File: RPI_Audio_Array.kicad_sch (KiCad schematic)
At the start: 40 parts, among them J1 Conn_02x20_Odd_Even, U1 PCMD3140IRTER, U2 SPH0690LM4H-1, U3 SPH0690LM4H-1, U4 SPH0690LM4H-1, U5 SPH0690LM4H-1, U6 TLV7103318QDSERQ1

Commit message: Fix: Schemtatic fixes
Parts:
- added C21, C22, C23, C24, C25: 2.2uf, Capacitor_SMD:C_0805_2012Metric, symbol Device:C
- added C26: 100nf, Capacitor_SMD:C_1206_3216Metric, symbol Device:C
- added C27: 1nf, Capacitor_SMD:C_0805_2012Metric, symbol Device:C
- added C28: 100pf, Capacitor_SMD:C_0805_2012Metric, symbol Device:C
- added C29: 10uf, Capacitor_SMD:C_1206_3216Metric, symbol Device:C
- added R3, R5: 470, Resistor_SMD:R_0201_0603Metric, symbol Device:R
- C11, C12, C5: lcsc (none) -> CL10C331JB8NNNC
- C13: value 1uf -> 10nf; footprint Capacitor_SMD:C_0603_1608Metric -> Capacitor_SMD:C_01005_0402Metric; lcsc CL10A105KB8NNNC -> CL05B103KB5NNNC
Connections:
- net VDD is gone; now on net +3.3V: U2.2 (SELECT), U4.2 (SELECT)
- net +3.3V: now also R3.2, R5.2; no longer U1.16 (AVDD)
- net +5V: now also C26.1, C27.1, C28.1, C29.1
- net GND: now also C21.2, C22.2, C23.2, C24.2, C25.2, C26.2, C27.2, C28.2, C29.2; no longer FB1.2
- net SCL: now also R5.1
- net SDA: now also R3.1
- net at C10.1, C12.1, C4.1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: now also C21.1
- net at C6.1, C7.1, C8.1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: now also C24.1
- net at C2.1, C3.1, C5.1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: now also C23.1
- net at C1.1, C11.1, C9.1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: now also C22.1
- new net AVDD: C25.1, FB1.2, U1.16 (AVDD)
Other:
- note added: "Bulk"
- note added: "Decoupling"
- moved on the sheet: C1, C10, C11, C12, C13, C4, C9, FB1, FB4, FB5, R8, R9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

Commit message: Chore: Updating PCB
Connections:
- net GPIO1 renamed PCMD_GPIO1
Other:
- note added: "Figure 3 shows SDOUT wired to SDIN of Pi"
- note added: "Shows PCM in is GPIO20"
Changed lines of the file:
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@@
   (junction (at 41.91 31.75) (diameter 0) (color 0 0 0 0)
-  )
-  (junction (at 143.51 110.49) (diameter 0) (color 0 0 0 0)
   )
   (no_connect (at 156.21 181.61))
@@
     (stroke (width 0) (type default))
   )
-  (wire (pts (xy 144.78 110.49) (xy 143.51 110.49))
-    (stroke (width 0) (type default))
-  )
   (wire (pts (xy 152.4 35.56) (xy 166.37 35.56))
     (stroke (width 0) (type default))
@@
     (stroke (width 0) (type default))
   )
+  (wire (pts (xy 139.7 110.49) (xy 143.51 110.49))
+    (stroke (width 0) (type default))
+  )
   (wire (pts (xy 25.4 99.06) (xy 33.02 99.06))
     (stroke (width 0) (type default))
@@
   )
   (wire (pts (xy 264.16 95.25) (xy 264.16 99.06))
-    (stroke (width 0) (type default))
-  )
-  (wire (pts (xy 143.51 110.49) (xy 139.7 110.49))
     (stroke (width 0) (type default))
   )
@@
     (effects (font (size 1.27 1.27)) (justify left bottom))
   )
+  (text "Figure 3 shows SDOUT wired to SDIN of Pi" (at 176.53 148.59 0)
+    (effects (font (size 1.27 1.27)) (justify left bottom) (href "https://www.analog.com/media/en/technical-documentation/technical-articles/ms-2275.pdf"))
+  )
+  (text "Shows PCM in is GPIO20" (at 176.53 152.4 0)
+    (effects (font (size 1.27 1.27)) (justify left bottom) (href "https://raspberrypi.stackexchange.com/questions/79870/confirming-the-i2s-pins-on-raspberry-pi-3-model-b"))
+  )
   (text "Decoupling" (at 25.4 151.13 0)
     (effects (font (size 1.27 1.27)) (justify left bottom))
@@
     )
   )
-  (global_label "GPIO1" (shape input) (at 231.14 107.95 0) (fields_autoplaced)
-    (effects (font (size 1.27 1.27)) (justify left))
-    (property "Intersheetrefs" "${INTERSHEET_REFS}" (at 239.81 107.95 0)
+  (global_label "PCMD_GPIO1" (shape input) (at 231.14 107.95 0) (fields_autoplaced)
+    (effects (font (size 1.27 1.27)) (justify left))
+    (property "Intersheetrefs" "${INTERSHEET_REFS}" (at 246.039 107.95 0)
       (effects (font (size 1.27 1.27)) (justify left) hide)
     )
@@
     )
   )
-  (global_label "GPIO1" (shape input) (at 143.51 181.61 180) (fields_autoplaced)
-    (effects (font (size 1.27 1.27)) (justify right))
-    (property "Intersheetrefs" "${INTERSHEET_REFS}" (at 134.84 181.61 0)
-      (effects (font (size 1.27 1.27)) (justify right) hide)
-    )
+  (global_label "PCMD_GPIO1" (shape input) (at 143.51 181.61 180) (fields_autoplaced)
+    (effects (font (size 1.27 1.27)) (justify right))
+    (property "Intersheetrefs" "${INTERSHEET_REFS}" (at 128.611 181.61 0)
+      (effects (font (size 1.27 1.27)) (justify right) hide)
+    )

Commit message: Fix: making further changes to bugs in schematic
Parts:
- added C30: 10uf, Capacitor_SMD:C_1206_3216Metric, symbol Device:C
- added C31, C35, C36: 100nf, Capacitor_SMD:C_1206_3216Metric, symbol Device:C
- added C32: 10nf, Capacitor_SMD:C_01005_0402Metric, symbol Device:C
- added C33: 1nf, Capacitor_SMD:C_0805_2012Metric, symbol Device:C
- added C34: 100pf, Capacitor_SMD:C_0805_2012Metric, symbol Device:C
- C25: value 2.2uf -> 100nf; footprint Capacitor_SMD:C_0805_2012Metric -> Capacitor_SMD:C_1206_3216Metric; lcsc CL21A225KBQNNNE -> CL31B104KBCNNNC
- R3, R5: value 470 -> 4K7
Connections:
- net +1V8: now also C30.1, C31.1, C32.1, C33.1, C34.1
- net +3.3V: now also C25.1; no longer C14.1, U2.2 (SELECT), U4.2 (SELECT)
- net +5V: no longer C13.1, C26.1, C27.1, C28.1, C29.1
- net AVDD: now also C13.1, C14.1, C26.1, C27.1, C28.1, C29.1, C36.1; no longer C25.1
- net GND: now also C30.2, C31.2, C32.2, C33.2, C34.2, C35.2, C36.2
- net SELECT_2: now reaches C24.1, C6.1, C7.1, C8.1, FB2.1, U2.5 (VDD)
- net SELECT_2: now also U2.2 (SELECT)
- net SELECT_1: now reaches C1.1, C11.1, C22.1, C9.1, FB4.1, U4.5 (VDD)
- net SELECT_1: now also U4.2 (SELECT)
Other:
- moved on the sheet: C13, C14, C15, C16, C17, C18, C19, C20, C26, C27, C28, C29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

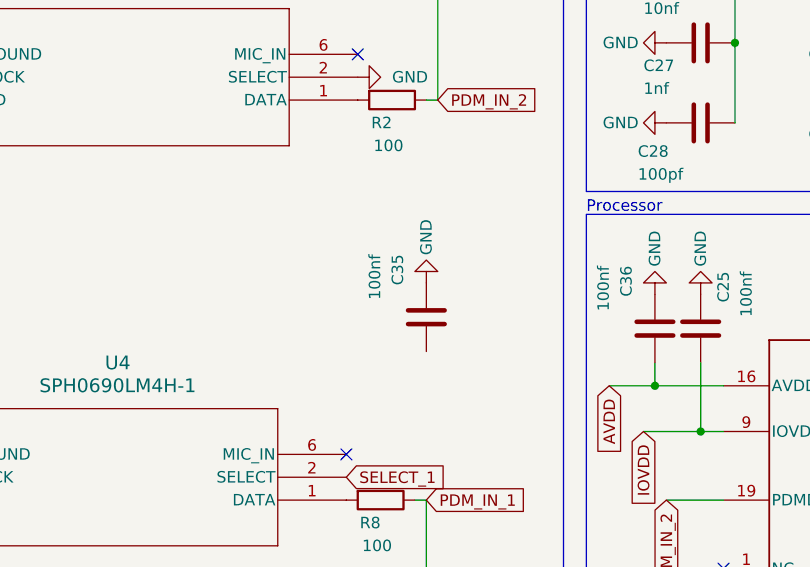
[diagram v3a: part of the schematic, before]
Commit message: Fix: Removing extra cap
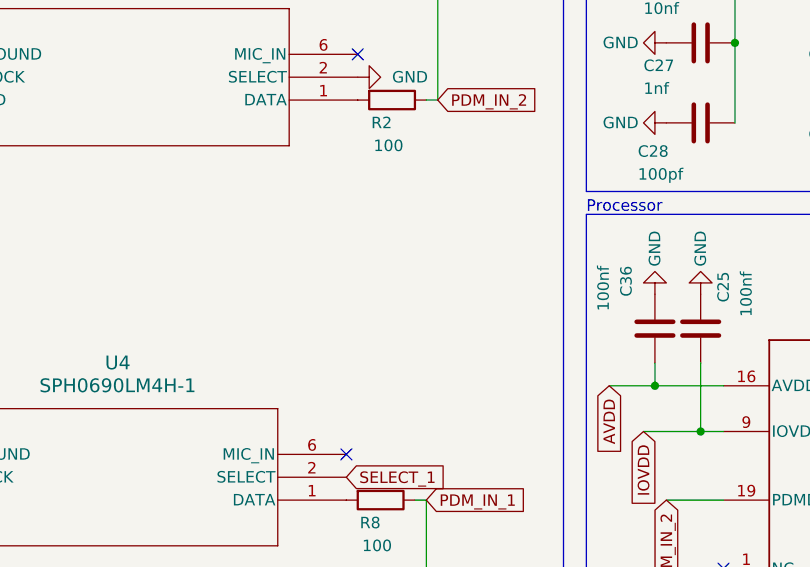
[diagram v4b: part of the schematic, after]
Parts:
- removed C35: 100nf, Capacitor_SMD:C_1206_3216Metric, symbol Device:C
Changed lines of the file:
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@@
-    )
-  )
-  (symbol (lib_id "power:GND") (at 110.49 74.93 180) (unit 1)
-    (in_bom yes) (on_board yes) (dnp no)
-    (property "Reference" "#PWR038" (at 110.49 68.58 0)
-      (effects (font (size 1.27 1.27)) hide)
-    )
-    (property "Value" "GND" (at 110.49 69.85 90)
-      (effects (font (size 1.27 1.27)))
-    )
-    (property "Footprint" "" (at 110.49 74.93 0)
-      (effects (font (size 1.27 1.27)) hide)
-    )
-    (property "Datasheet" "" (at 110.49 74.93 0)
-      (effects (font (size 1.27 1.27)) hide)
-    )
-    (pin "1")
-    (instances
-      (project "RPI_Audio_Array"
-        (path "/954bfd10-59e4-4b5e-a9fc-5f77bd6479b0"
-          (reference "#PWR038") (unit 1)
-        )
-      )
     )
   )
@@
         )
       )
-    )
-  )
-  (symbol (lib_id "Device:C") (at 110.49 78.74 180) (unit 1)
-    (in_bom yes) (on_board yes) (dnp no)
-    (property "Reference" "C35" (at 107.315 71.755 90)
-      (effects (font (size 1.27 1.27)) (justify left))
-    )
-    (property "Value" "100nf" (at 104.775 71.755 90)
-      (effects (font (size 1.27 1.27)) (justify left))
-    )
-    (property "Footprint" "Capacitor_SMD:C_1206_3216Metric" (at 109.5248 74.93 0)
-      (effects (font (size 1.27 1.27)) hide)
-    )
-    (property "Datasheet" "https://jlcpcb.com/partdetail/25237-CL31B104KBCNNNC/C24497" (at 110.49 78.74 0)
-      (effects (font (size 1.27 1.27)) hide)
-    )
-    (property "lcsc" "CL31B104KBCNNNC" (at 110.49 78.74 0)
-      (effects (font (size 1.27 1.27)) hide)
-    )
-    (pin "1")
-    (pin "2")
-    (instances
-      (project "RPI_Audio_Array"
-        (path "/954bfd10-59e4-4b5e-a9fc-5f77bd6479b0"
-          (reference "C35") (unit 1)
-        )
-      )

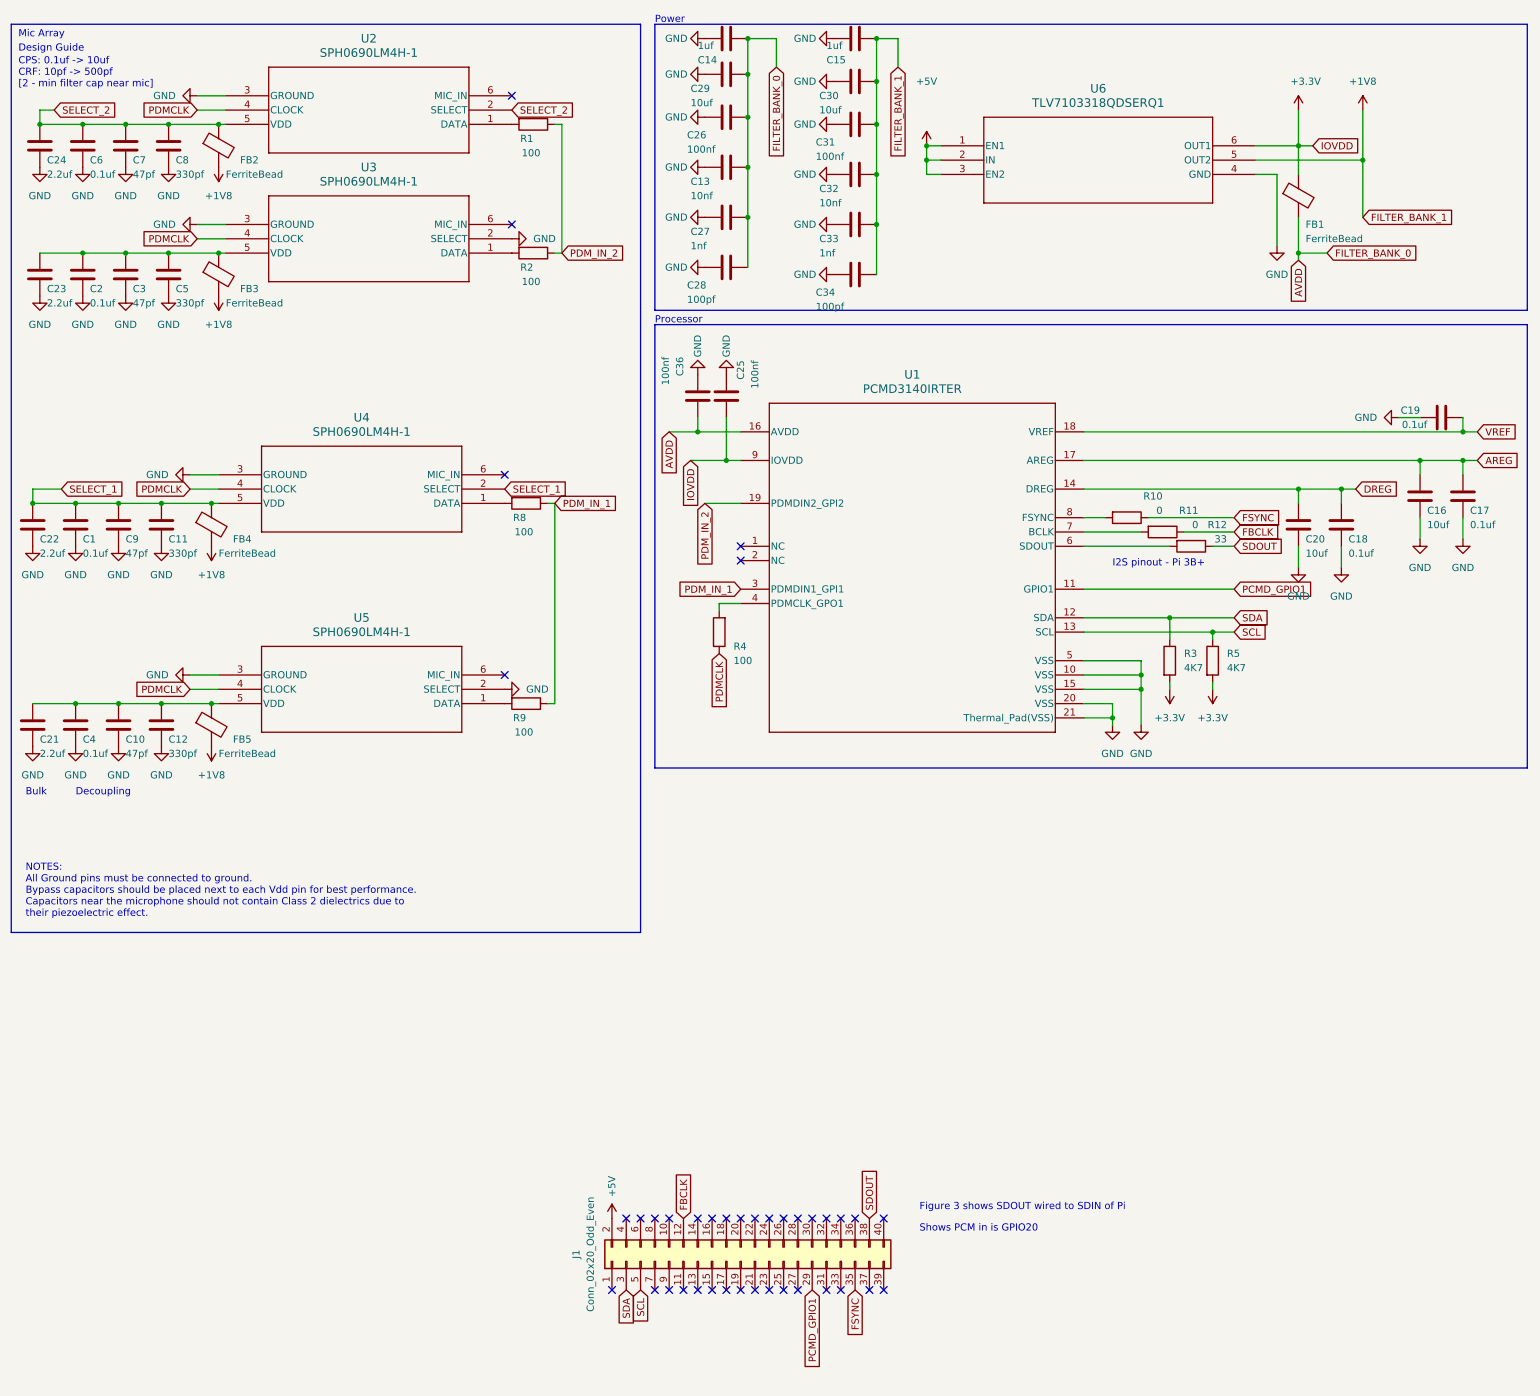
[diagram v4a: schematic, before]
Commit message: Chore: To fix drc issues
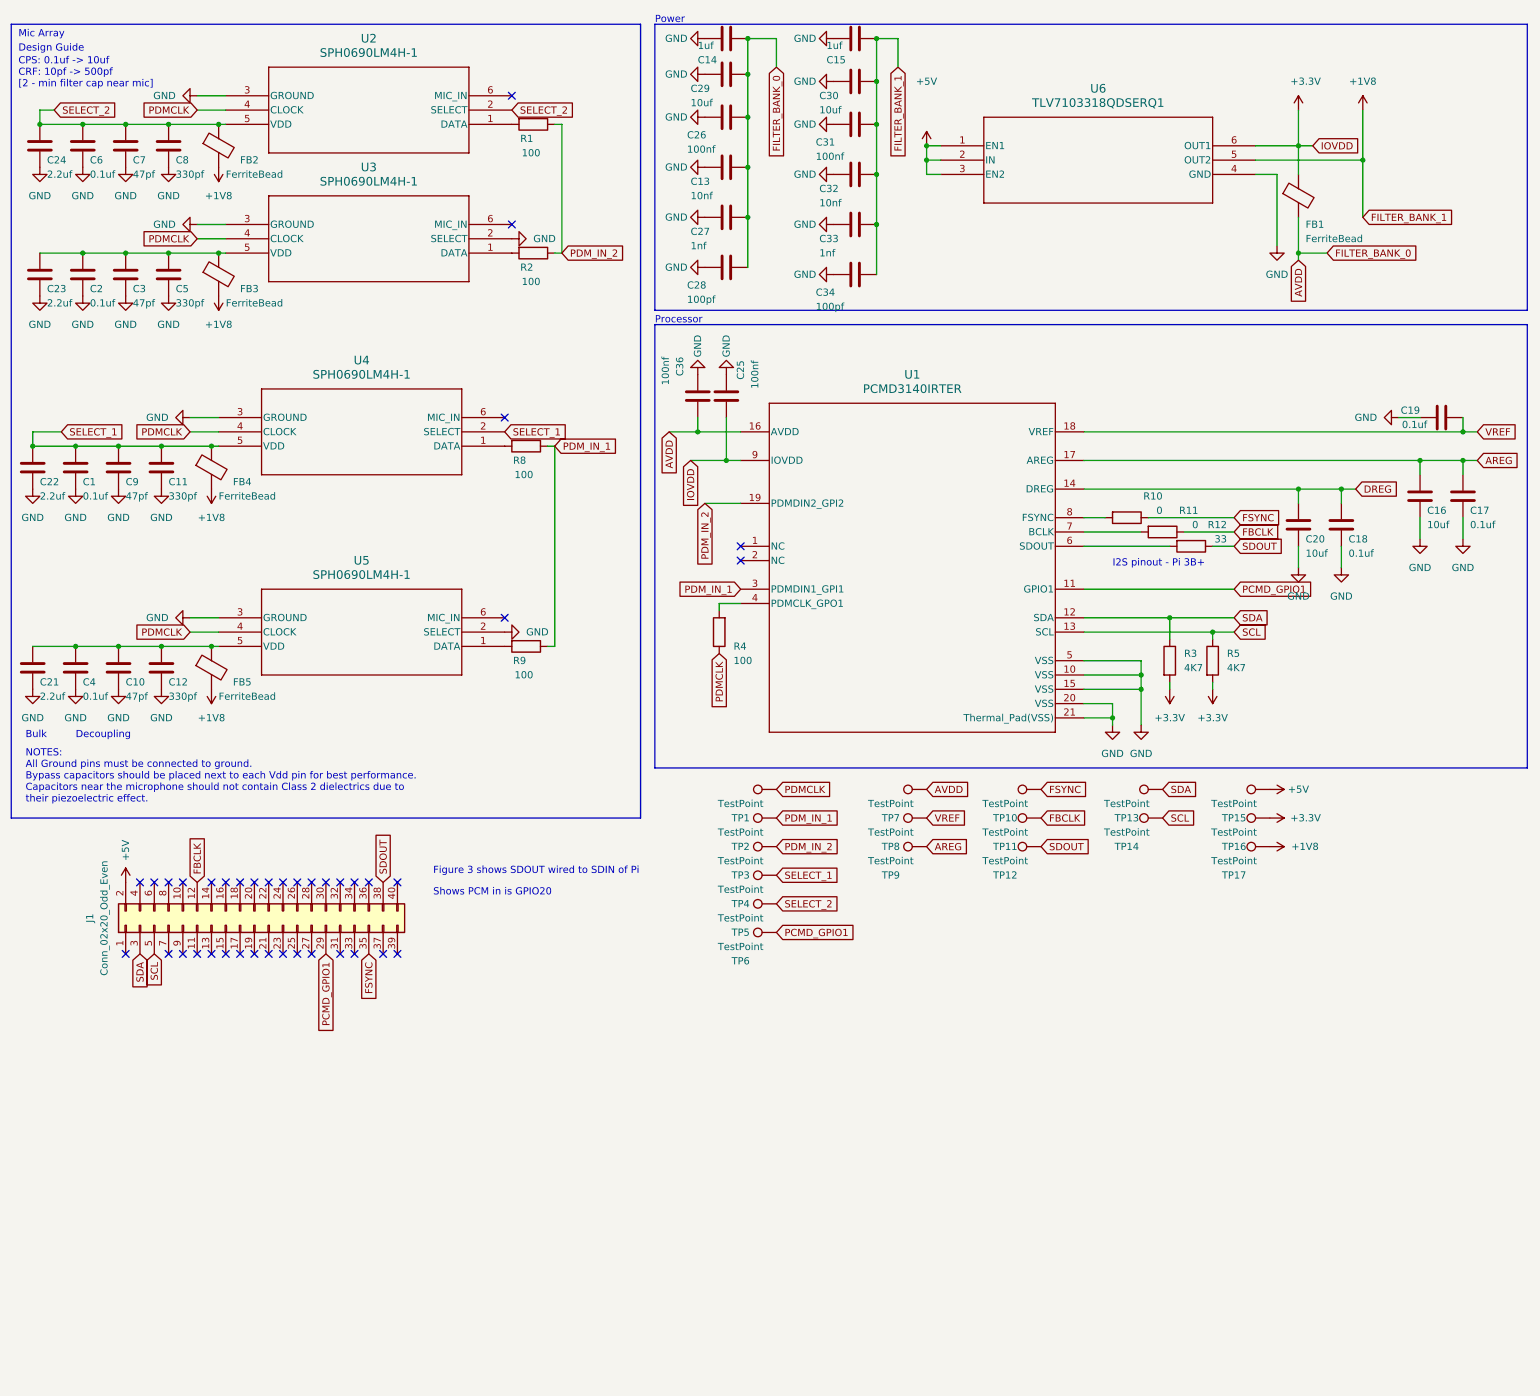
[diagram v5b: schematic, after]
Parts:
- added TP1, TP10, TP11, TP12, TP13, TP14, TP15, TP16, TP17, TP2, TP3, TP4, TP5, TP6, TP7, TP8, TP9: TestPoint, TestPoint:TestPoint_Plated_Hole_D2.0mm, symbol Connector:TestPoint
- C1, C17, C18, C2, C4, C6: footprint Capacitor_SMD:C_01005_0402Metric -> Capacitor_SMD:C_0603_1608Metric; lcsc CL05B104KB54PNC -> CC0603KRX7R9BB104
- R3, R5: footprint Resistor_SMD:R_0201_0603Metric -> Resistor_SMD:R_0603_1608Metric
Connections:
- net +1V8: now also TP17.1
- net +3.3V: now also TP16.1
- net +5V: now also TP15.1
- net AREG: now also TP9.1
- net AVDD: now also TP7.1
- net FBCLK: now also TP11.1
- net FSYNC: now also TP10.1
- net PCMD_GPIO1: now also TP6.1
- net PDMCLK: now also TP1.1
- net PDM_IN_1: now also TP2.1
- net PDM_IN_2: now also TP3.1
- net SCL: now also TP14.1
- net SDA: now also TP13.1
- net SDOUT: now also TP12.1
- net SELECT_1: now also TP4.1
- net SELECT_2: now also TP5.1
- net VREF: now also TP8.1
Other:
- moved on the sheet: C1, C10, C11, C12, C21, C22, C4, C9, FB4, FB5, J1, R8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
